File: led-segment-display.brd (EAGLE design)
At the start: 20 x 34 mm, 42 parts

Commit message: led-segment-display : Change to 15 segment display
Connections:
- removed net N$12: LED17.C, LED18.A
- removed net N$4: LED5.C, LED6.A
- removed net N$8: LED11.C, LED12.A
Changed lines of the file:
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@@
 <wire x1="17.3" y1="33.5" x2="14.1" y2="33.5" width="0" layer="19" extent="1-1"/>
-</signal>
-<signal name="N$4">
-<contactref element="LED5" pad="C"/>
-<contactref element="LED6" pad="A"/>
-<wire x1="12.3" y1="33.5" x2="9.1" y2="33.5" width="0" layer="19" extent="1-1"/>
 </signal>
 <signal name="N$5">
@@
 <wire x1="17.3" y1="17.5" x2="14.1" y2="17.5" width="0" layer="19" extent="1-1"/>
 </signal>
-<signal name="N$8">
-<contactref element="LED11" pad="C"/>
-<contactref element="LED12" pad="A"/>
-<wire x1="12.3" y1="17.5" x2="9.1" y2="17.5" width="0" layer="19" extent="1-1"/>
-</signal>
 <signal name="N$9">
 <contactref element="LED13" pad="C"/>
@@
 <wire x1="17.3" y1="1.5" x2="14.1" y2="1.5" width="0" layer="19" extent="1-1"/>
 </signal>
-<signal name="N$12">
-<contactref element="LED17" pad="C"/>
-<contactref element="LED18" pad="A"/>
-<wire x1="12.3" y1="1.5" x2="9.1" y2="1.5" width="0" layer="19" extent="1-1"/>
-</signal>
 <signal name="N$15">

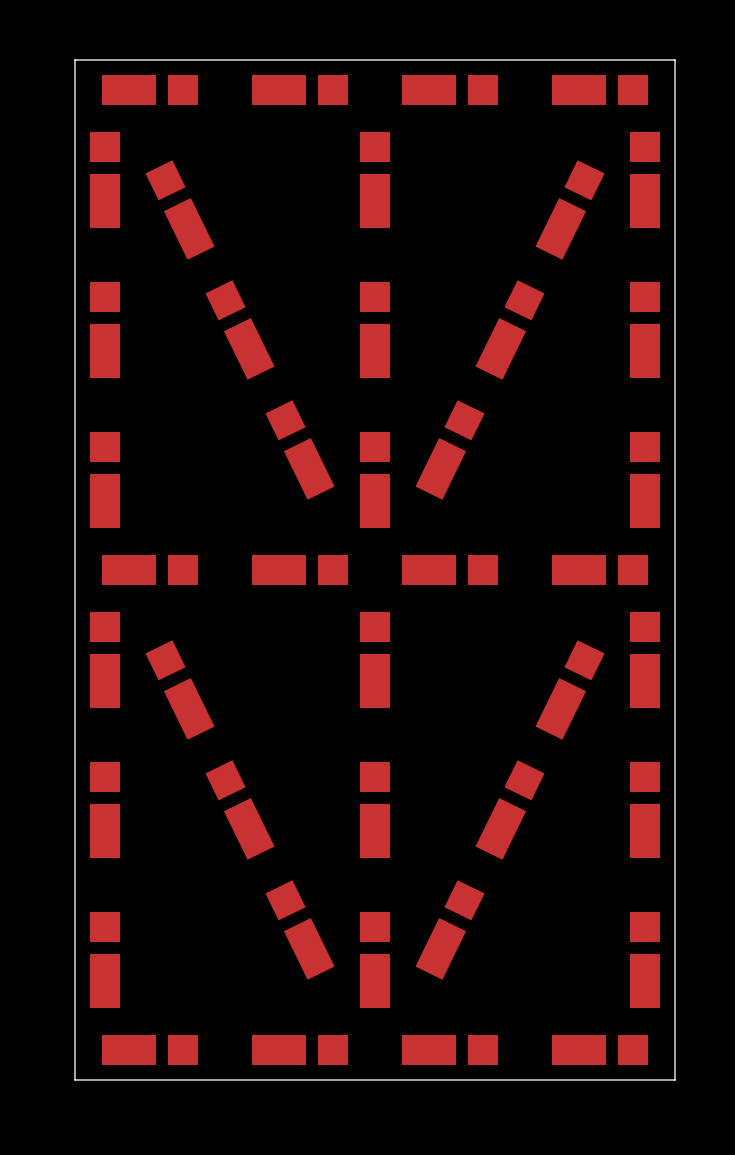
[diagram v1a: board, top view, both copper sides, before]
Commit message: led-segment-display : fixed error in diagonal, reduced vertical size
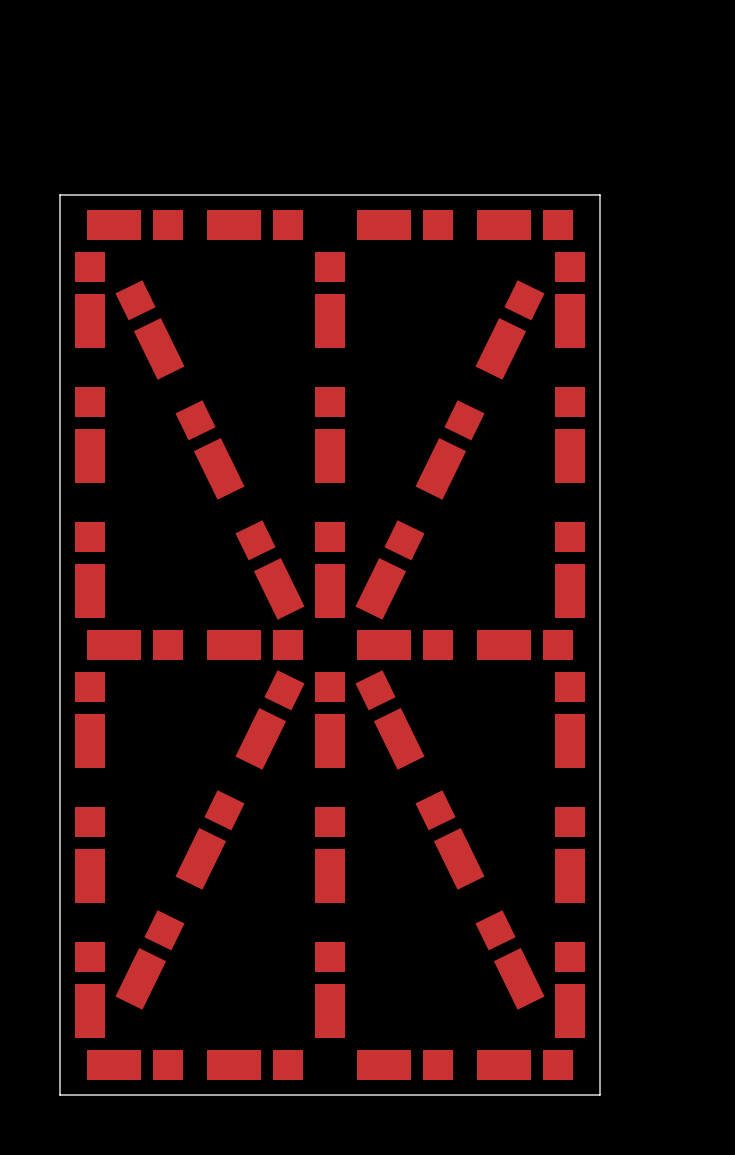
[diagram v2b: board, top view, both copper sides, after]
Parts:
- moved LED34 6.08 mm to (11.0, 12.5), turned to 116 degrees
- moved LED4 5.15 mm to (15.5, 29.0)
- moved LED36 5.10 mm to (3.00, 4.50), turned to 64 degrees
- moved LED5 4.74 mm to (11.5, 29.0)
- moved LED6 4.74 mm to (6.50, 29.0)
- moved LED7 4.72 mm to (17.0, 26.5)
- moved LED40 4.53 mm to (2.50, 29.0)
- moved LED30 4.47 mm to (15.0, 25.5)
- moved LED31 4.47 mm to (13.0, 21.5)
- moved LED38 4.47 mm to (11.0, 17.5)
- moved LED8 4.30 mm to (17.0, 22.0)
- moved LED22 4.27 mm to (9.00, 26.5)
- moved LED28 4.12 mm to (3.00, 25.5)
- moved LED29 4.12 mm to (5.00, 21.5)
- moved LED37 4.12 mm to (7.00, 17.5)
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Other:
- board size 20 x 34 mm -> 18 x 30 mm

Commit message: led-sgement-display : as sent to oshpark
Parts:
- added C1: 1uF, SparkFun-Capacitors:1206-CAP
- added C2: 2.2uF, SparkFun-Capacitors:1206-CAP
- added D1: MBRA140, SparkFun-DiscreteSemi:SMA-DIODE
- added J1: (no value), mechanical:2X3_SMD_2.54MM
- added J3: 1x3 RA Female .1", mechanical:1X3_SMD_2.54MM
- added L1: 33uH, SparkFun-Passives:SRN6045
- added LED43, LED44, LED45, LED46, LED47, LED48: (no value), semiconductors:LED-3014
- added R2: 0.3R, SparkFun-Resistors:0805
- added U1: AL8805, SparkFun-PowerIC:SOT23-5
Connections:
- new net CTRL_CH1: J1.3, J1.4, J3.2, U1.3
- new net GND: C2.2, J1.5, J1.6, J3.3, U1.2
- new net I_A: C1.1, LED1.A, LED12.A, LED13.A, LED18.A, LED19.A, LED22.A, LED25.A, LED28.A, LED30.A, LED32.A, LED34.A, LED43.A, LED45.A, LED47.A, LED6.A, LED7.A, R2.2, U1.4
- new net I_C: C1.2, L1.2, LED11.C, LED15.C, LED17.C, LED21.C, LED24.C, LED27.C, LED3.C, LED36.C, LED37.C, LED38.C, LED39.C, LED44.C, LED46.C, LED48.C, LED5.C, LED9.C
- new net N$12: LED42.C, LED48.A
- new net N$34: LED16.A, LED47.C
- new net N$35: LED10.A, LED45.C
- new net N$36: LED41.C, LED46.A
- new net N$4: LED4.A, LED43.C
- new net N$8: LED40.C, LED44.A
- new net SW: D1.A, L1.1, U1.1
- new net VIN: C2.1, D1.C, J1.1, J1.2, J3.1, R2.1, U1.5
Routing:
- net I_A: track 0.00 -> 75.5 mm, vias 0 -> 9
- net I_C: track 0.00 -> 72.8 mm, vias 0 -> 8
- net CTRL_CH1: track 0.00 -> 38.3 mm, vias 0 -> 2
- net VIN: track 0.00 -> 31.7 mm, vias 0 -> 2
- net GND: track 0.00 -> 24.3 mm
- net N$9: track 0.00 -> 2.70 mm
- net N$17: track 0.00 -> 2.70 mm
- net N$13: track 0.00 -> 2.70 mm
- net N$18: track 0.00 -> 2.70 mm
- net N$14: track 0.00 -> 2.70 mm
- net N$10: track 0.00 -> 2.70 mm
- net N$6: track 0.00 -> 2.70 mm
- net N$5: track 0.00 -> 2.70 mm
- net N$2: track 0.00 -> 2.70 mm
- net N$16: track 0.00 -> 2.70 mm
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- added copper zone on layer 1, net I_A
- added copper zone on layer 1, net I_C
- added copper zone on layer 16, net SW
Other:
- board text added: "V1.0"
